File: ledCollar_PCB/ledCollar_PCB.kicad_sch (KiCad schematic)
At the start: 40 parts, among them J1 PWR+, J2 PWR-, J3 APA102, J6 SWD, Q1 AO3400A, Q2 Senba SMD0805-20, SW1 SW_Push, U1 AP2112K-3.3, U2 STM32F103C8Tx, U3 NRF24L01_Breakout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

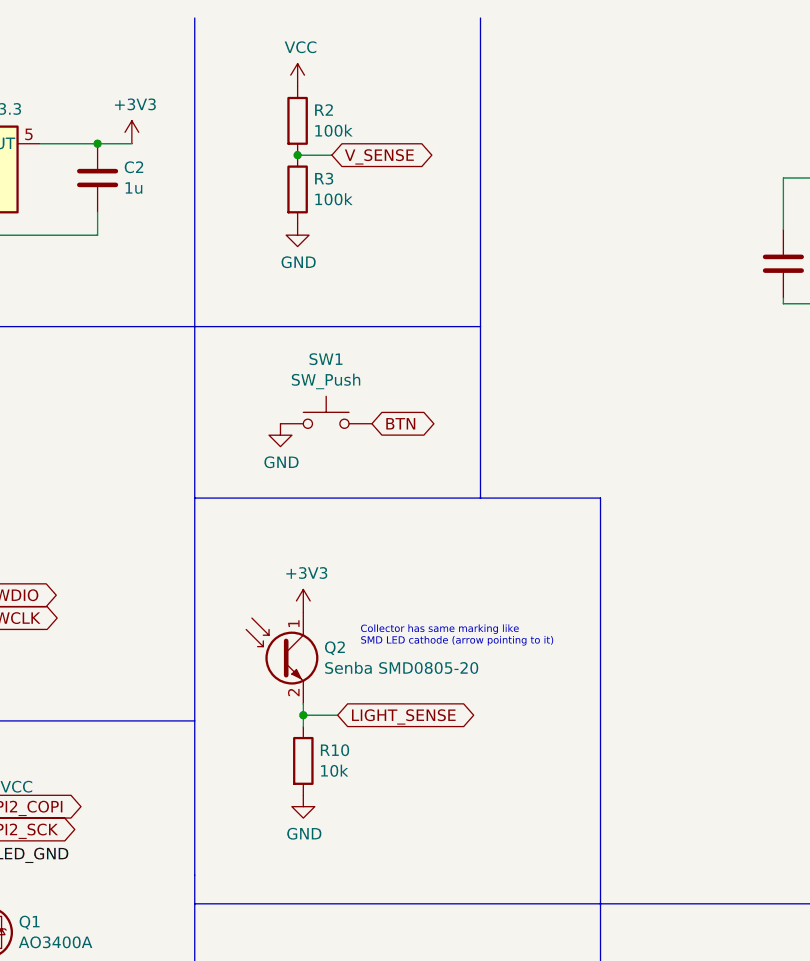
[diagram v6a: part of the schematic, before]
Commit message: add ADC input bypass caps
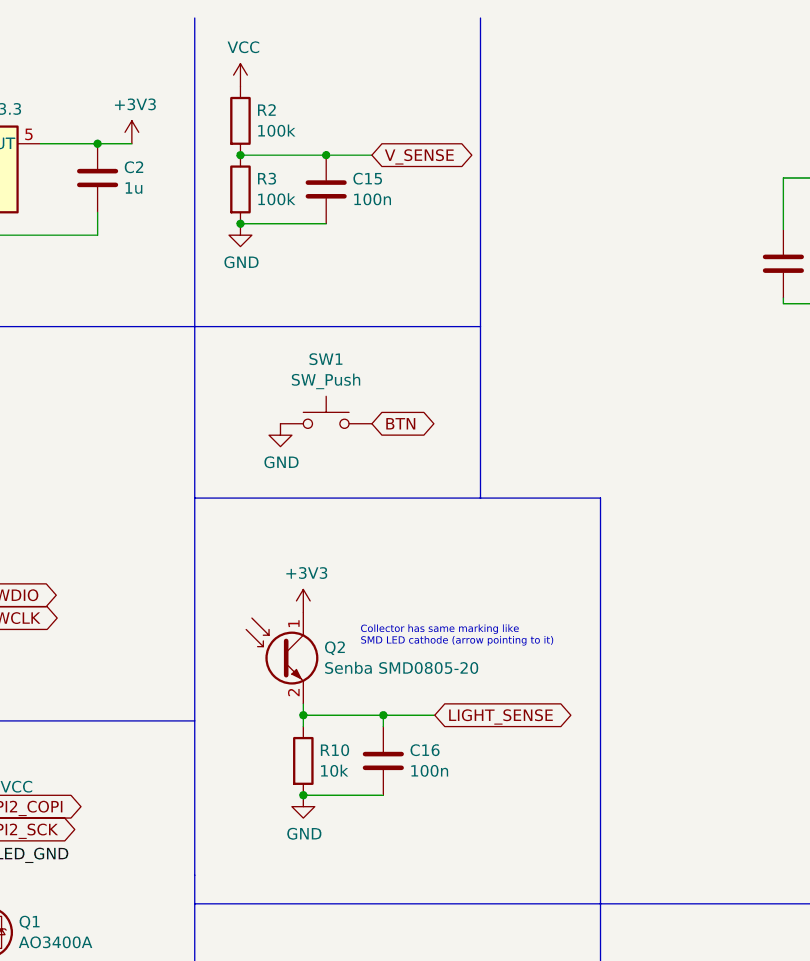
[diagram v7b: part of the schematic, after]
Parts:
- added C15, C16: 100n, Capacitor_SMD:C_0603_1608Metric, symbol Device:C
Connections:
- net GND: now also C15.1, C16.1
- net LIGHT_SENSE: now also C16.2
- net V_SENSE: now also C15.2
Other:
- moved on the sheet: R2, R3
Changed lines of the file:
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@@
   (junction (at 54.61 26.035) (diameter 0) (color 0 0 0 0))
   (junction (at 54.61 166.37) (diameter 0) (color 0 0 0 0))
+  (junction (at 70.485 27.305) (diameter 0) (color 0 0 0 0))
+  (junction (at 70.485 34.925) (diameter 0) (color 0 0 0 0))
   (junction (at 72.39 143.51) (diameter 0) (color 0 0 0 0))
-  (junction (at 76.835 27.305) (diameter 0) (color 0 0 0 0))
   (junction (at 77.47 89.535) (diameter 0) (color 0 0 0 0))
+  (junction (at 77.47 98.425) (diameter 0) (color 0 0 0 0))
+  (junction (at 80.01 27.305) (diameter 0) (color 0 0 0 0))
+  (junction (at 86.36 89.535) (diameter 0) (color 0 0 0 0))
   (junction (at 102.87 171.45) (diameter 0) (color 0 0 0 0))
   (junction (at 135.89 43.815) (diameter 0) (color 0 0 0 0))
@@
     (stroke (width 0) (type solid) (color 0 0 0 0))
   )
+  (wire (pts (xy 70.485 27.305) (xy 80.01 27.305))
+    (stroke (width 0) (type solid) (color 0 0 0 0))
+  )
+  (wire (pts (xy 70.485 34.925) (xy 80.01 34.925))
+    (stroke (width 0) (type solid) (color 0 0 0 0))
+  )
   (wire (pts (xy 72.39 143.51) (xy 74.93 143.51))
     (stroke (width 0) (type solid) (color 0 0 0 0))
   )
-  (wire (pts (xy 76.835 27.305) (xy 80.645 27.305))
-    (stroke (width 0) (type solid) (color 0 0 0 0))
-  )
   (wire (pts (xy 77.47 88.265) (xy 77.47 89.535))
     (stroke (width 0) (type solid) (color 0 0 0 0))
@@
     (stroke (width 0) (type solid) (color 0 0 0 0))
   )
-  (wire (pts (xy 77.47 89.535) (xy 81.28 89.535))
+  (wire (pts (xy 77.47 89.535) (xy 86.36 89.535))
+    (stroke (width 0) (type solid) (color 0 0 0 0))
+  )
+  (wire (pts (xy 77.47 98.425) (xy 86.36 98.425))
+    (stroke (width 0) (type solid) (color 0 0 0 0))
+  )
+  (wire (pts (xy 80.01 27.305) (xy 85.09 27.305))
+    (stroke (width 0) (type solid) (color 0 0 0 0))
+  )
+  (wire (pts (xy 86.36 89.535) (xy 86.36 90.805))
+    (stroke (width 0) (type solid) (color 0 0 0 0))
+  )
+  (wire (pts (xy 86.36 89.535) (xy 92.075 89.535))
     (stroke (width 0) (type solid) (color 0 0 0 0))
   )
@@
     (effects (font (size 1.27 1.27)) (justify left))
   )
-  (global_label "V_SENSE" (shape bidirectional) (at 80.645 27.305 0)
-    (effects (font (size 1.27 1.27)) (justify left))
-  )
-  (global_label "LIGHT_SENSE" (shape bidirectional) (at 81.28 89.535 0)
+  (global_label "V_SENSE" (shape bidirectional) (at 85.09 27.305 0)
     (effects (font (size 1.27 1.27)) (justify left))
   )
@@
     (effects (font (size 1.27 1.27)) (justify left))
   )
+  (global_label "LIGHT_SENSE" (shape bidirectional) (at 92.075 89.535 0)
+    (effects (font (size 1.27 1.27)) (justify left))
+  )
   (global_label "LIGHT_SENSE" (shape bidirectional) (at 149.86 57.785 180)
     (effects (font (size 1.27 1.27)) (justify right))
@@
     )
   )
+  (symbol (lib_id "power:VCC") (at 70.485 19.685 0)
+    (in_bom yes) (on_board yes)
+    (property "Reference" "#PWR0123" (id 0) (at 70.485 23.495 0)
+      (effects (font (size 1.27 1.27)) hide)
+    )
+    (property "Value" "VCC" (id 1) (at 70.8533 15.3606 0))
+    (property "Footprint" "" (id 2) (at 70.485 19.685 0)
+      (effects (font (size 1.27 1.27)) hide)
+    )
+    (property "Datasheet" "" (id 3) (at 70.485 19.685 0)
+      (effects (font (size 1.27 1.27)) hide)
+    )
+  )
   (symbol (lib_id "power:+3V3") (at 72.39 143.51 0)
     (in_bom yes) (on_board yes)
@@
     )
   )
-  (symbol (lib_id "power:VCC") (at 76.835 19.685 0)
-    (in_bom yes) (on_board yes)
-    (property "Reference" "#PWR0123" (id 0) (at 76.835 23.495 0)
-      (effects (font (size 1.27 1.27)) hide)
-    )
-    (property "Value" "VCC" (id 1) (at 77.2033 15.3606 0))
-    (property "Footprint" "" (id 2) (at 76.835 19.685 0)
-      (effects (font (size 1.27 1.27)) hide)
-    )
-    (property "Datasheet" "" (id 3) (at 76.835 19.685 0)
-      (effects (font (size 1.27 1.27)) hide)
-    )
-  )
   (symbol (lib_id "power:+3V3") (at 77.47 78.105 0)
     (in_bom yes) (on_board yes)
@@
     )
   )
+  (symbol (lib_id "power:GND") (at 70.485 34.925 0)
+    (in_bom yes) (on_board yes)
+    (property "Reference" "#PWR0122" (id 0) (at 70.485 41.275 0)
+      (effects (font (size 1.27 1.27)) hide)
+    )
+    (property "Value" "GND" (id 1) (at 70.5993 39.2494 0))
+    (property "Footprint" "" (id 2) (at 70.485 34.925 0)
+      (effects (font (size 1.27 1.27)) hide)
+    )
+    (property "Datasheet" "" (id 3) (at 70.485 34.925 0)
+      (effects (font (size 1.27 1.27)) hide)
+    )
+  )
   (symbol (lib_id "power:GND") (at 72.39 179.07 0)
     (in_bom yes) (on_board yes)
@@
     )
   )
-  (symbol (lib_id "power:GND") (at 76.835 34.925 0)
-    (in_bom yes) (on_board yes)
-    (property "Reference" "#PWR0122" (id 0) (at 76.835 41.275 0)
-      (effects (font (size 1.27 1.27)) hide)
-    )
-    (property "Value" "GND" (id 1) (at 76.9493 39.2494 0))
-    (property "Footprint" "" (id 2) (at 76.835 34.925 0)
-      (effects (font (size 1.27 1.27)) hide)
-    )
-    (property "Datasheet" "" (id 3) (at 76.835 34.925 0)
-      (effects (font (size 1.27 1.27)) hide)
-    )
-  )
   (symbol (lib_id "power:GND") (at 77.47 98.425 0)
     (in_bom yes) (on_board yes)
@@
     )
   )
-  (symbol (lib_id "Device:R") (at 76.835 23.495 0)
-    (in_bom yes) (on_board yes)
-    (property "Reference" "R2" (id 0) (at 78.6131 22.3456 0)
-      (effects (font (size 1.27 1.27)) (justify left))
-    )
-    (property "Value" "100k" (id 1) (at 78.613 24.644 0)
-      (effects (font (size 1.27 1.27)) (justify left))
-    )
-    (property "Footprint" "Resistor_SMD:R_0603_1608Metric" (id 2) (at 75.057 23.495 90)
-      (effects (font (size 1.27 1.27)) hide)
-    )
-    (property "Datasheet" "~" (id 3) (at 76.835 23.495 0)
-      (effects (font (size 1.27 1.27)) hide)
-    )
-  )
-  (symbol (lib_id "Device:R") (at 76.835 31.115 0)
-    (in_bom yes) (on_board yes)
-    (property "Reference" "R3" (id 0) (at 78.6131 29.9656 0)
-      (effects (font (size 1.27 1.27)) (justify left))
-    )
-    (property "Value" "100k" (id 1) (at 78.613 32.264 0)
-      (effects (font (size 1.27 1.27)) (justify left))
-    )
-    (property "Footprint" "Resistor_SMD:R_0603_1608Metric" (id 2) (at 75.057 31.115 90)
-      (effects (font (size 1.27 1.27)) hide)
-    )
-    (property "Datasheet" "~" (id 3) (at 76.835 31.115 0)
+  (symbol (lib_id "Device:R") (at 70.485 23.495 0)
+    (in_bom yes) (on_board yes)
+    (property "Reference" "R2" (id 0) (at 72.2631 22.3456 0)
+      (effects (font (size 1.27 1.27)) (justify left))
+    )
+    (property "Value" "100k" (id 1) (at 72.263 24.644 0)
+      (effects (font (size 1.27 1.27)) (justify left))
+    )
+    (property "Footprint" "Resistor_SMD:R_0603_1608Metric" (id 2) (at 68.707 23.495 90)
+      (effects (font (size 1.27 1.27)) hide)
+    )
+    (property "Datasheet" "~" (id 3) (at 70.485 23.495 0)
+      (effects (font (size 1.27 1.27)) hide)
+    )
+  )
+  (symbol (lib_id "Device:R") (at 70.485 31.115 0)
+    (in_bom yes) (on_board yes)
+    (property "Reference" "R3" (id 0) (at 72.2631 29.9656 0)
+      (effects (font (size 1.27 1.27)) (justify left))
+    )
+    (property "Value" "100k" (id 1) (at 72.263 32.264 0)
+      (effects (font (size 1.27 1.27)) (justify left))
+    )
+    (property "Footprint" "Resistor_SMD:R_0603_1608Metric" (id 2) (at 68.707 31.115 90)
+      (effects (font (size 1.27 1.27)) hide)
+    )
+    (property "Datasheet" "~" (id 3) (at 70.485 31.115 0)
       (effects (font (size 1.27 1.27)) hide)
     )
@@
     )
   )
+  (symbol (lib_id "Device:C") (at 80.01 31.115 180) (unit 1)
+    (in_bom yes) (on_board yes)
+    (property "Reference" "C15" (id 0) (at 82.9311 29.9656 0)
+      (effects (font (size 1.27 1.27)) (justify right))
+    )
+    (property "Value" "100n" (id 1) (at 82.931 32.264 0)
+      (effects (font (size 1.27 1.27)) (justify right))
+    )
+    (property "Footprint" "Capacitor_SMD:C_0603_1608Metric" (id 2) (at 79.0448 27.305 0)
+      (effects (font (size 1.27 1.27)) hide)
+    )
+    (property "Datasheet" "~" (id 3) (at 80.01 31.115 0)
+      (effects (font (size 1.27 1.27)) hide)
+    )
+  )
   (symbol (lib_id "Device:C") (at 81.28 138.43 0)
     (in_bom yes) (on_board yes)
@@
     )
     (property "Datasheet" "~" (id 3) (at 81.28 138.43 0)
+      (effects (font (size 1.27 1.27)) hide)
+    )
+  )
+  (symbol (lib_id "Device:C") (at 86.36 94.615 180) (unit 1)
+    (in_bom yes) (on_board yes)
+    (property "Reference" "C16" (id 0) (at 89.2811 93.4656 0)
+      (effects (font (size 1.27 1.27)) (justify right))
+    )
+    (property "Value" "100n" (id 1) (at 89.281 95.764 0)
+      (effects (font (size 1.27 1.27)) (justify right))
+    )
+    (property "Footprint" "Capacitor_SMD:C_0603_1608Metric" (id 2) (at 85.3948 90.805 0)
+      (effects (font (size 1.27 1.27)) hide)
+    )
+    (property "Datasheet" "~" (id 3) (at 86.36 94.615 0)
       (effects (font (size 1.27 1.27)) hide)
     )
@@
       (reference "C14") (unit 1)
     )
+    (path "/837de216-143c-49e0-8bf0-829275c17aad"
+      (reference "C15") (unit 1)
+    )
+    (path "/1e6b4df2-3c62-416c-993c-92b57842fae4"
+      (reference "C16") (unit 1)
+    )
     (path "/1e18a7f3-1069-4097-b796-5dffa9df0099"
